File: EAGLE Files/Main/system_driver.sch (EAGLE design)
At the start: 12 parts

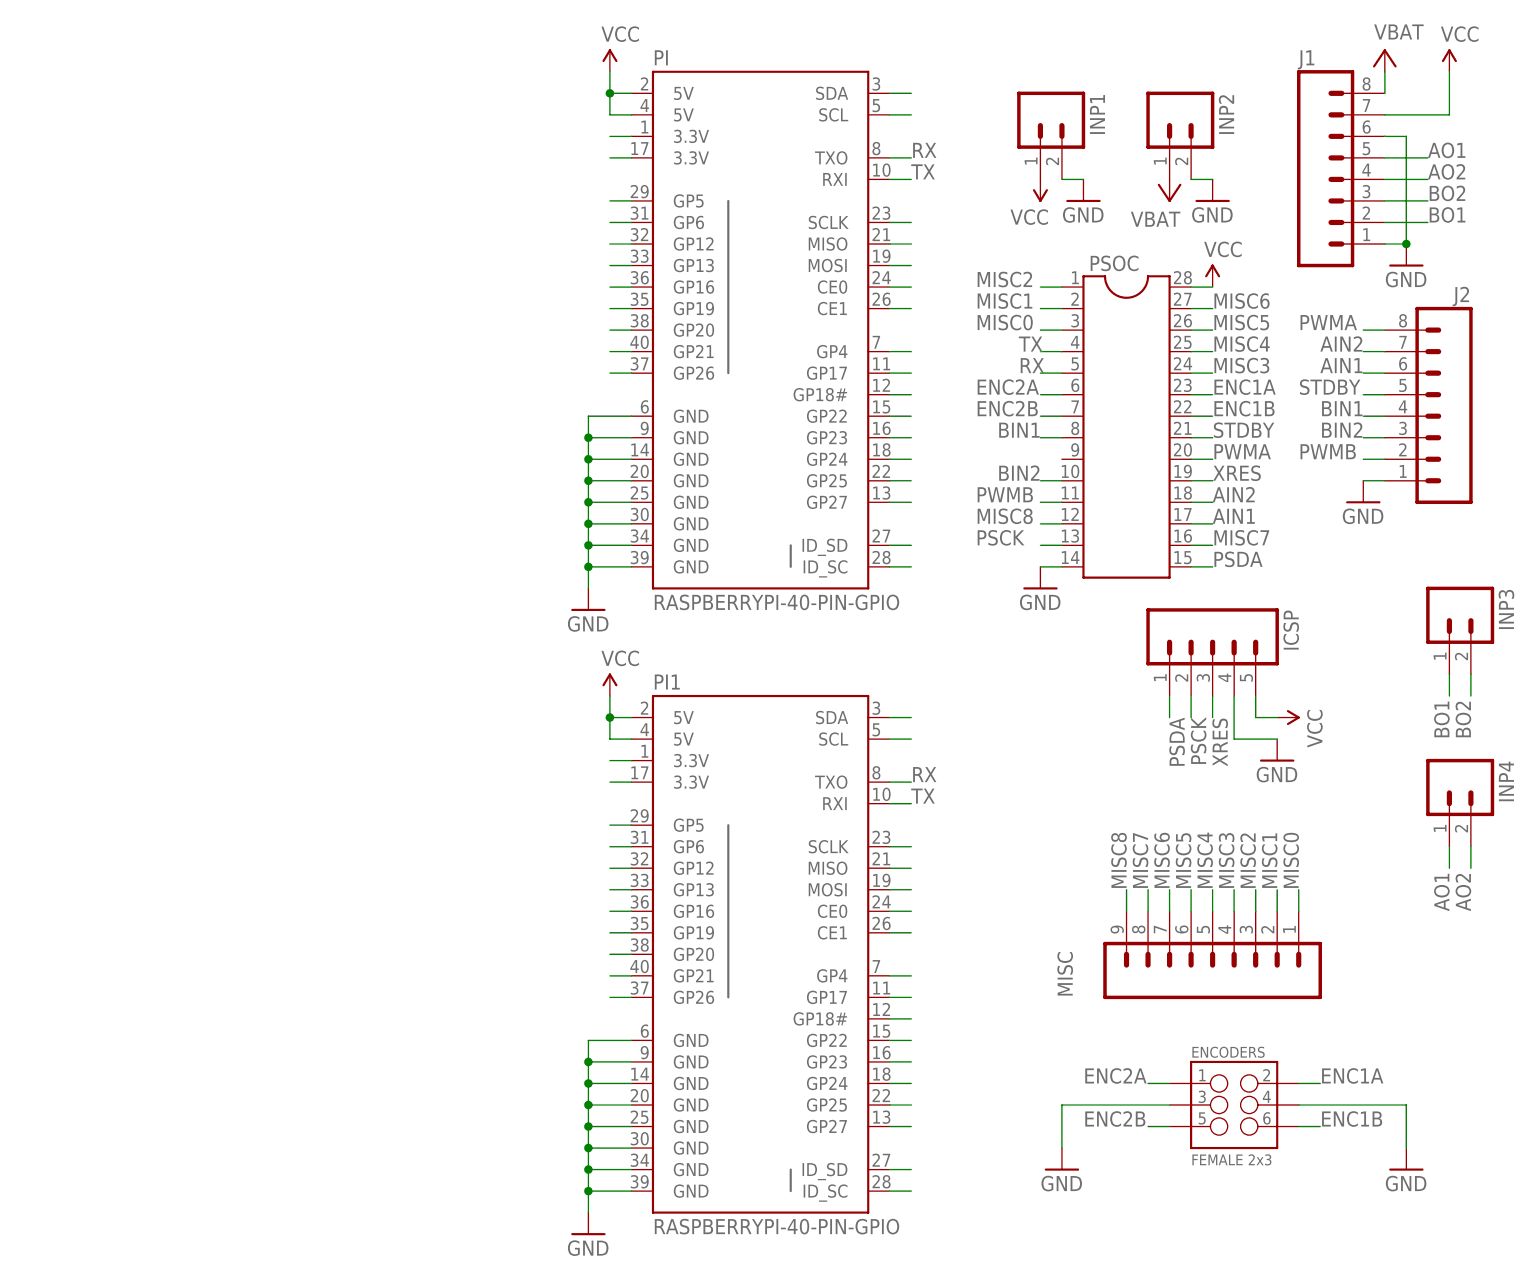
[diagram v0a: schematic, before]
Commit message: updated EAGLE files
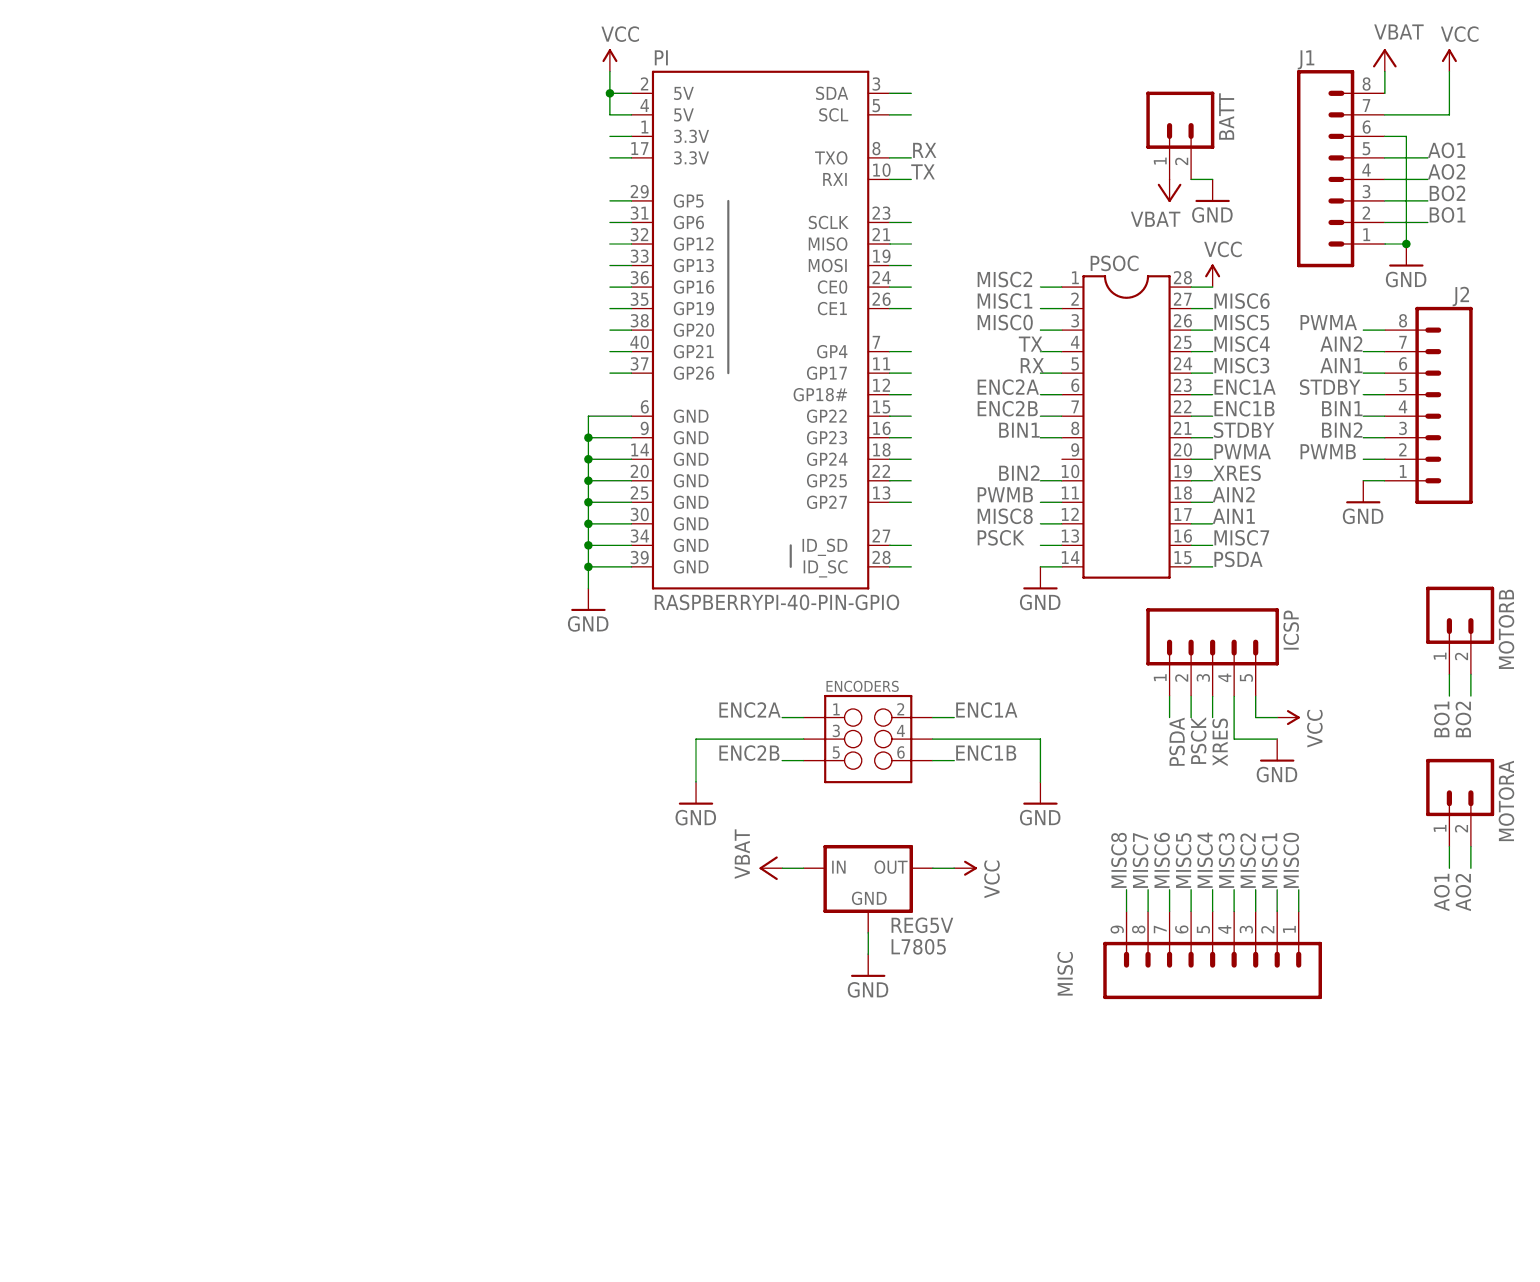
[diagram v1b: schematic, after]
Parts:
- removed INP1: (no value), SparkFun-Connectors:M02LOCK_LONGPADS
- removed PI1: RASPBERRYPI-40-PIN-GPIO, SparkFun-Boards:RASPBERRYPI-40-PIN-GPIO
- added REG5V: L7805, SparkFun-PowerIC:V_REG_LD1117VXX
- ENCODERS: value FEMALE 2x3 -> (none)
- renumbered INP2 to BATT, INP3 to MOTORB, INP4 to MOTORA
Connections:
- net 3.3V: no longer PI1.3.3V@1, PI1.3.3V@17
- net CE0: no longer PI1.CE0
- net CE1: no longer PI1.CE1
- net GND: now also REG5V.GND; no longer INP1.2, PI1.GND@14, PI1.GND@20, PI1.GND@25, PI1.GND@30, PI1.GND@34, PI1.GND@39, PI1.GND@6, PI1.GND@9
- net GP12: no longer PI1.GP12
- net GP13: no longer PI1.GP13
- net GP16: no longer PI1.GP16
- net GP17: no longer PI1.GP17
- net GP18: no longer PI1.GP18#
- net GP19: no longer PI1.GP19
- net GP20: no longer PI1.GP20
- net GP21: no longer PI1.GP21
- net GP22: no longer PI1.GP22
- net GP23: no longer PI1.GP23
- net GP24: no longer PI1.GP24
- net GP25: no longer PI1.GP25
- net GP26: no longer PI1.GP26
- net GP27: no longer PI1.GP27
- net GP4: no longer PI1.GP4
- net GP5: no longer PI1.GP5
- net GP6: no longer PI1.GP6
- net ID_SC: no longer PI1.ID_SC
- net ID_SD: no longer PI1.ID_SD
- net MISO: no longer PI1.MISO
- net MOSI: no longer PI1.MOSI
- net PI_SCL: no longer PI1.SCL
- net PI_SDA: no longer PI1.SDA
- net RX: no longer PI1.TXO
- net SCLK: no longer PI1.SCLK
- net TX: no longer PI1.RXI
- net V+: now also REG5V.IN
- net VCC: now also REG5V.OUT; no longer INP1.1, PI1.5V@2, PI1.5V@4
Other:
- moved on the sheet: ENCODERS
